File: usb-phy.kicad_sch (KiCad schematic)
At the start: 105 parts, among them J12 614004184726, J13 USB4105-GF-A, J14 USB4105-GF-A, Q17 BSS138PW, U15 TPS7B8133DRVR, U16 TPD4E05U06QDQARQ1, U17 TPD4E05U06QDQARQ1, U18 SN74HC595D, U19 MAX3421EETJ+, U20 FT4232H-56Q, U21 TPD4E05U06QDQARQ1, U22 TXU0304BQAR, U23 TXU0304BQAR, U24 TXU0304BQAR, U25 TUSB1106RSVR, Y1 ABM8G-12.000MHZ-18-D2Y-T, Y2 ABM8G-12.000MHZ-18-D2Y-T

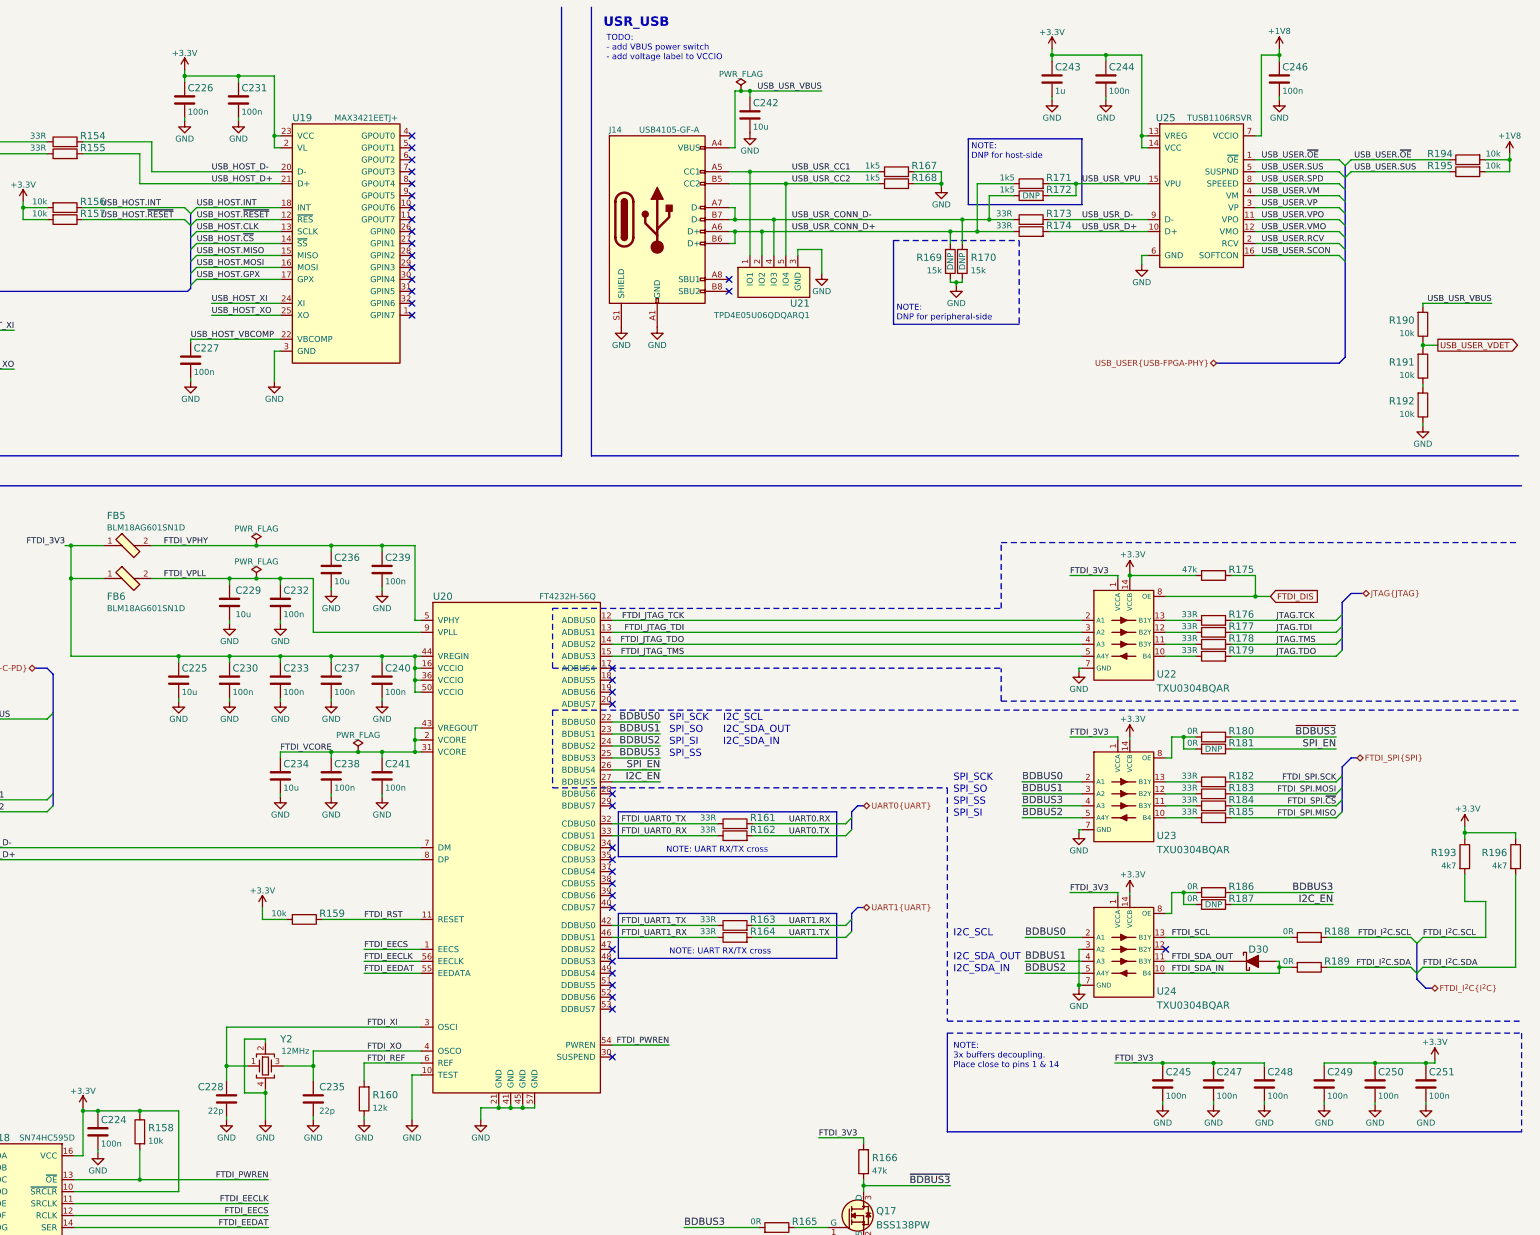
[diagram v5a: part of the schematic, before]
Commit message: Replace 100n to 0402
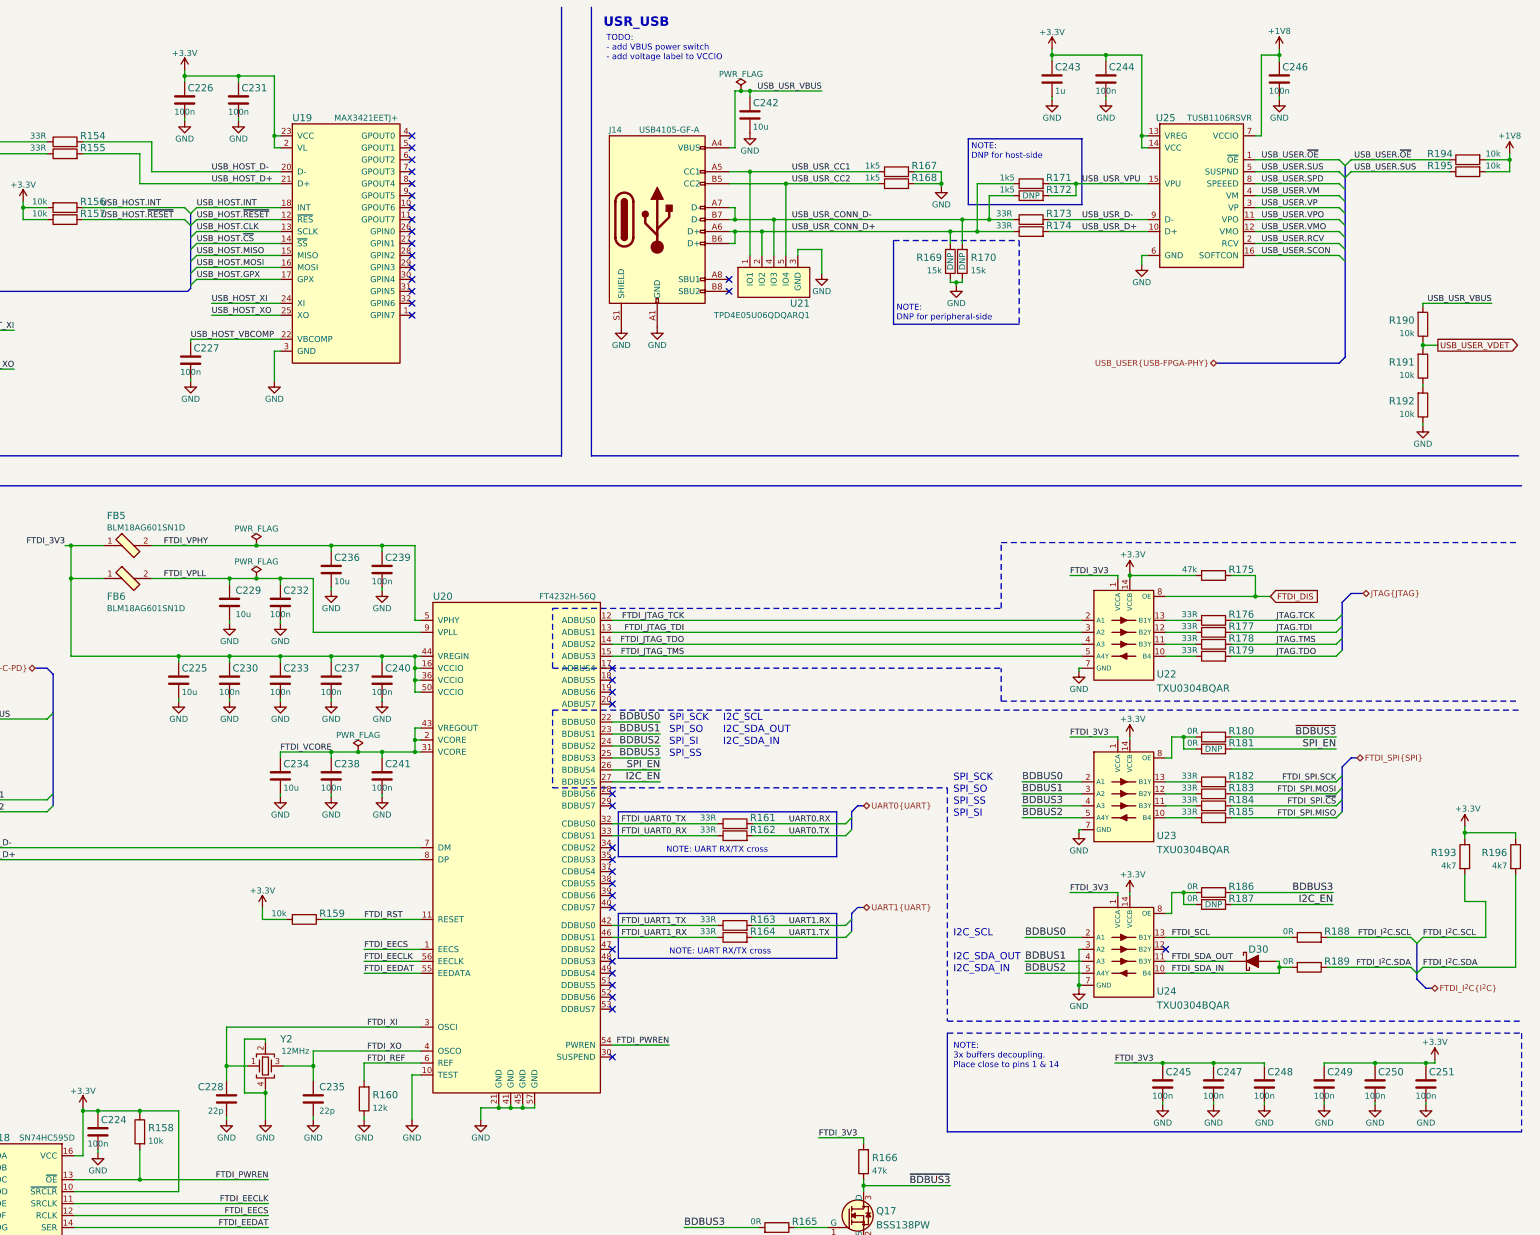
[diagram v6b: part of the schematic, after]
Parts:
- C224, C226, C227, C230, C231, C232, C233, C237, C238, C239, C240, C241, C244, C245, C246, C247, C248, C249, C250, C251: value C_100n_0201 -> C_100n_0402_EIA; footprint antmicro-footprints:0201-res -> antmicro-footprints:0402-cap_EIA; symbol antmicroCapacitorsmisc:C_100n_0201 -> antmicroCapacitors0402:C_100n_0402_EIA; MPN CC0201KRX6S5BB104 -> GRM155R61H104KE14D; Manufacturer YAGEO -> Murata

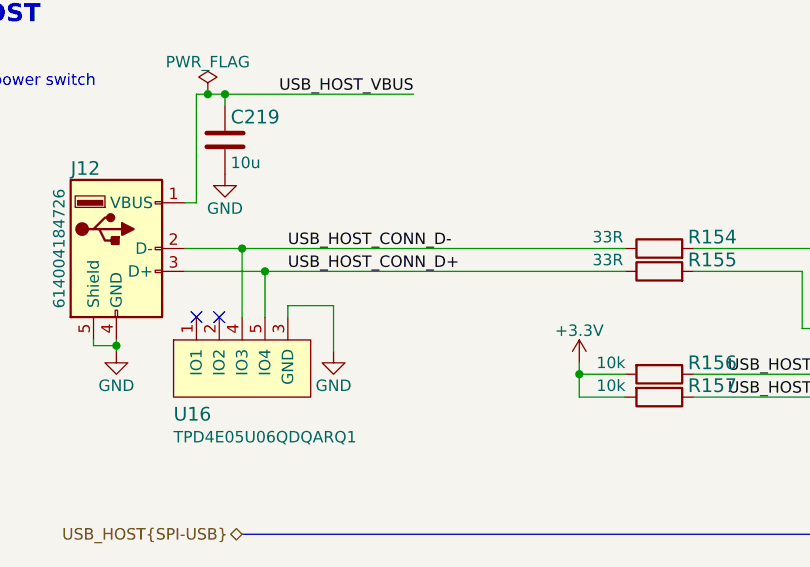
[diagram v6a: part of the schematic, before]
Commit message: Fix minor label missmatch. Continue placment
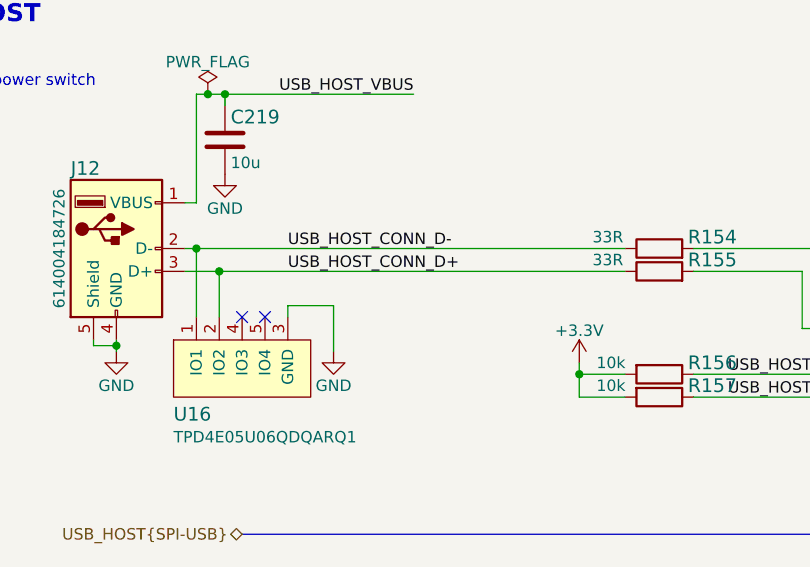
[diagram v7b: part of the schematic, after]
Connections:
- net USB_HOST_CONN_D+: now also U16.2 (IO2), U16.9 (IO2); no longer U16.5 (IO4), U16.6 (IO4)
- net USB_HOST_CONN_D-: now also U16.1 (IO1), U16.10 (IO1); no longer U16.4 (IO3), U16.7 (IO3)
- new net: U16.4 (IO3), U16.7 (IO3)
- new net: U16.5 (IO4), U16.6 (IO4)
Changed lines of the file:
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@@
   (junction (at 37.465 52.705) (diameter 0) (color 0 0 0 0)
   )
-  (junction (at 53.975 44.45) (diameter 0) (color 0 0 0 0)
-  )
   (junction (at 140.335 243.84) (diameter 0) (color 0 0 0 0)
   )
@@
   (junction (at 189.865 247.015) (diameter 0) (color 0 0 0 0)
   )
-  (junction (at 51.435 41.91) (diameter 0) (color 0 0 0 0)
-  )
   (junction (at 318.77 23.495) (diameter 0) (color 0 0 0 0)
   )
@@
   (junction (at 132.715 151.13) (diameter 0) (color 0 0 0 0)
   )
+  (junction (at 48.895 44.45) (diameter 0) (color 0 0 0 0)
+  )
   (junction (at 335.28 201.295) (diameter 0) (color 0 0 0 0)
   )
@@
   )
   (junction (at 165.1 151.13) (diameter 0) (color 0 0 0 0)
+  )
+  (junction (at 46.355 41.91) (diameter 0) (color 0 0 0 0)
   )
   (junction (at 172.085 153.67) (diameter 0) (color 0 0 0 0)
@@
   (no_connect (at 171.45 60.96))
   (no_connect (at 213.995 223.52))
-  (no_connect (at 46.355 49.53))
+  (no_connect (at 51.435 49.53))
   (no_connect (at 55.88 204.47))
   (no_connect (at 79.375 262.255))
@@
   (no_connect (at 171.45 78.74))
   (no_connect (at 79.375 259.715))
-  (no_connect (at 48.895 49.53))
+  (no_connect (at 53.975 49.53))
   (bus_entry (at 125.73 55.88) (size -1.27 1.27)
     (stroke (width 0) (type default) (color 0 0 0 0))
@@
   )
   (wire (pts (xy 365.125 237.49) (xy 365.125 238.125))
-    (stroke (width 0) (type default) (color 0 0 0 0))
-  )
-  (wire (pts (xy 45.085 41.91) (xy 51.435 41.91))
     (stroke (width 0) (type default) (color 0 0 0 0))
   )
@@
     (stroke (width 0) (type default) (color 0 0 0 0))
   )
-  (wire (pts (xy 45.085 44.45) (xy 53.975 44.45))
-    (stroke (width 0) (type default) (color 0 0 0 0))
-  )
   (wire (pts (xy 326.39 40.64) (xy 327.66 40.64))
     (stroke (width 0) (type default) (color 0 0 0 0))
@@
     (stroke (width 0) (type default) (color 0 0 0 0))
   )
-  (wire (pts (xy 53.975 44.45) (xy 53.975 49.53))
-    (stroke (width 0) (type default) (color 0 0 0 0))
-  )
   (wire (pts (xy 345.44 203.835) (xy 367.03 203.835))
     (stroke (width 0) (type default) (color 0 0 0 0))
@@
     (stroke (width 0) (type default) (color 0 0 0 0))
   )
-  (wire (pts (xy 51.435 41.91) (xy 51.435 49.53))
-    (stroke (width 0) (type default) (color 0 0 0 0))
-  )
   (polyline (pts (xy 313.69 41.275) (xy 289.56 41.275))
     (stroke (width 0) (type default) (color 0 0 0 0))
   )
+  (wire (pts (xy 48.895 44.45) (xy 93.98 44.45))
+    (stroke (width 0) (type default) (color 0 0 0 0))
+  )
   (wire (pts (xy 125.73 71.12) (xy 143.51 71.12))
     (stroke (width 0) (type default) (color 0 0 0 0))
@@
     (stroke (width 0) (type default) (color 0 0 0 0))
   )
-  (wire (pts (xy 51.435 41.91) (xy 93.98 41.91))
+  (wire (pts (xy 45.085 41.91) (xy 46.355 41.91))
     (stroke (width 0) (type default) (color 0 0 0 0))
   )
@@
     (stroke (width 0) (type default) (color 0 0 0 0))
   )
+  (wire (pts (xy 46.355 41.91) (xy 93.98 41.91))
+    (stroke (width 0) (type default) (color 0 0 0 0))
+  )
   (wire (pts (xy 20.32 261.62) (xy 20.32 267.97))
     (stroke (width 0) (type default) (color 0 0 0 0))
@@
     (stroke (width 0) (type default) (color 0 0 0 0))
   )
-  (wire (pts (xy 53.975 44.45) (xy 93.98 44.45))
+  (wire (pts (xy 45.085 44.45) (xy 48.895 44.45))
     (stroke (width 0) (type default) (color 0 0 0 0))
   )
@@
   )
   (wire (pts (xy 355.6 217.17) (xy 355.6 215.9))
+    (stroke (width 0) (type default) (color 0 0 0 0))
+  )
+  (wire (pts (xy 46.355 41.91) (xy 46.355 49.53))
     (stroke (width 0) (type default) (color 0 0 0 0))
   )
@@
     (stroke (width 0) (type default) (color 0 0 0 0))
   )
+  (wire (pts (xy 48.895 44.45) (xy 48.895 49.53))
+    (stroke (width 0) (type default) (color 0 0 0 0))
+  )
